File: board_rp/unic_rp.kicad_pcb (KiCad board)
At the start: 4 copper layers, 50 x 15.2 mm, 207 parts, among them J2 USB_C_Receptacle, Q1 2N7002, Q10 2N7002, Q11 2N7002, Q12 2N7002, Q13 2N7002, Q14 2N7002, Q15 2N7002, Q16 2N7002, Q17 2N7002, Q18 2N7002, Q19 2N7002, Q2 2N7002, Q20 2N7002, Q21 2N7002, Q22 2N7002, Q23 2N7002, Q24 2N7002, Q25 2N7002, Q26 2N7002, Q27 2N7002, Q28 2N7002, Q29 2N7002, Q3 2N7002, Q30 2N7002, Q31 2N7002, Q32 2N7002, Q33 2N7002, Q34 2N7002, Q35 2N7002, Q36 2N7002, Q37 2N7002, Q38 2N7002, Q39 2N7002, Q4 2N7002, Q40 2N7002, Q41 2N7002, Q42 AO3401A, Q43 2N7002, Q5 2N7002, Q6 2N7002, Q7 2N7002, Q8 2N7002, Q9 2N7002, U1 RP2350_80QFN, U10 ESD224DQA, U2 ESD224DQA, U3 MIC5203-3.3BM5, U4 APS6404L-3SQR-ZR, U5 TMUX154ERSW, U6 AP62150Z6, U7 W25Q16JVUXIQ, U8 LM393, U9 74AUP1G08, X1 27MHz

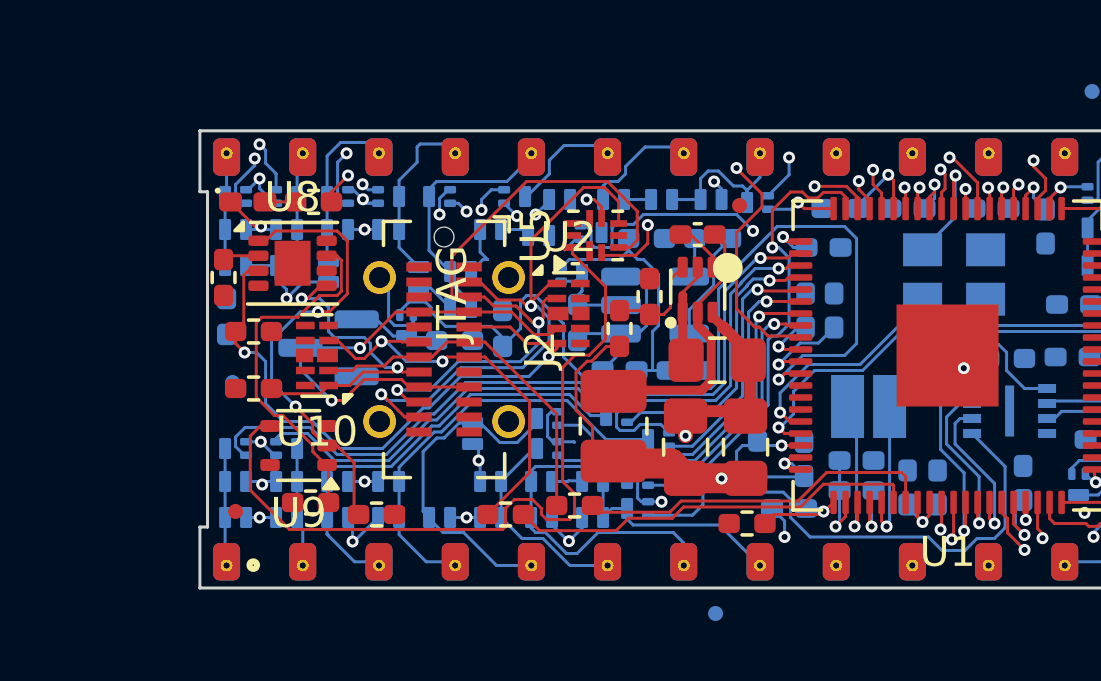
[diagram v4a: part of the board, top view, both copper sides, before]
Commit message: More or less complete schematic.
Component selection is not final, but functionality around
USB-C connector is. We even have UART output on it now as
well as USB VBUS detection and control on the right pins.
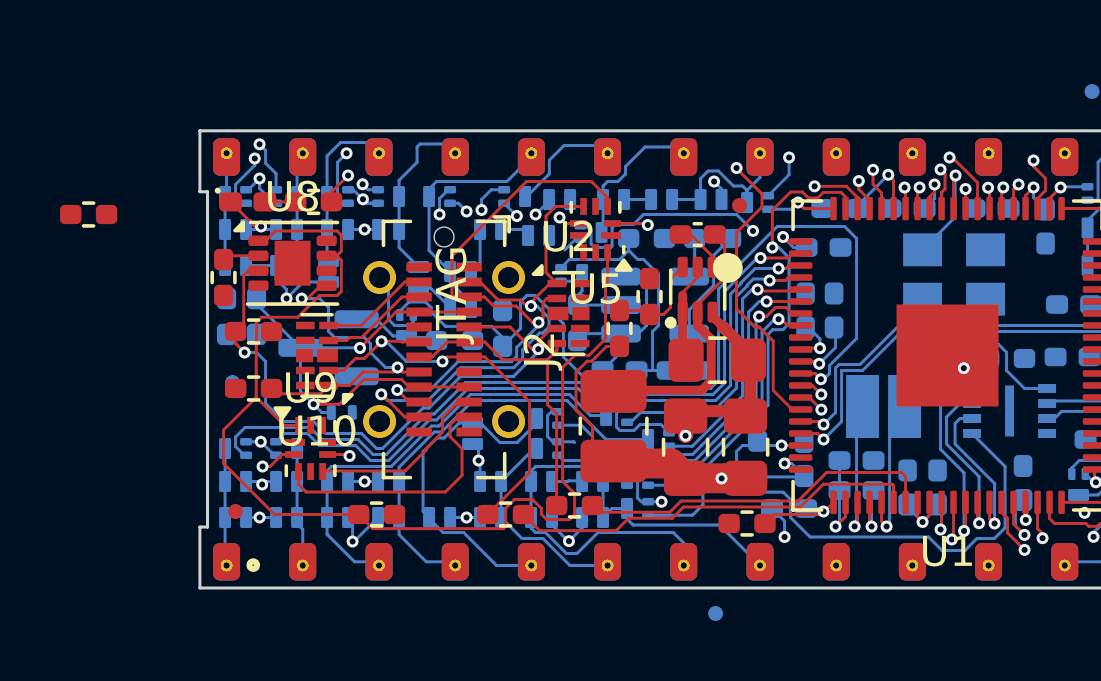
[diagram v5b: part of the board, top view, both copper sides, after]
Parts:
- added R27: 10k, UNIC:R_0402_1005Metric_Pad0.72x0.64mm_HandSolder, F.Cu at (34.6, 57.9)
- added U11: TPD1E05U06DPY, Package_SON:Texas_DPY0002A_0.6x1mm_P0.65mm, B.Cu at (43.0, 64.5)
- R23: value 10k -> 1k; moved to B.Cu
- U9: value 74AUP1G08 -> TMUX154ERSW; footprint Package_TO_SOT_SMD:SOT-353_SC-70-5 -> Package_DFN_QFN:UQFN-10_1.4x1.8mm_P0.4mm
- moved R23 6.46 mm to (40.2, 61.3), turned to 90 degrees
- moved L2 0.50 mm to (61.1, 64.3)
- moved U9 0.41 mm to (42.0, 65.7), turned to 0 degrees
- moved U5 0.20 mm to (51.5, 58.4), turned to 180 degrees
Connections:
- J2 pad A10: unconnected-(J2-RX2--PadA10) -> /USB_RXM
- J2 pad A11: unconnected-(J2-RX2+-PadA11) -> /USB_RXP
- J2 pad A2: /USB_TXM -> /USB_TXP
- J2 pad A3: /USB_TXP -> /USB_TXM
- J2 pad B10: unconnected-(J2-RX1--PadB10) -> /USB_RXM
- J2 pad B11: unconnected-(J2-RX1+-PadB11) -> /USB_RXP
- J2 pad B2: /USB_TXM -> /USB_TXP
- J2 pad B3: /USB_TXP -> /USB_TXM
- R1 pad 1: Net-(U1-GPIO40_ADC0) -> /LED_OUT
- R23 pad 1: +3V3 -> Net-(U1-GPIO40_ADC0)
- R23 pad 2: Net-(R23-Pad2) -> /VBUS
- R24 pad 2: Net-(R24-Pad2) -> Net-(U5-SEL)
- U1 pad 53: unconnected-(U1-GPIO42_ADC2-Pad53) -> /UART_TX
- U1 pad 54: unconnected-(U1-GPIO43_ADC3-Pad54) -> /UART_RX
- U1 pad 55: unconnected-(U1-GPIO44_ADC4-Pad55) -> /LED_OUT
- U10 pad 2: /USB_DP -> /USB_DM
- U10 pad 4: /USB_DM -> /USB_RXM
- U10 pad 5: unconnected-(U10-Pad5) -> /USB_RXP
- U2 pad 1: /USB_TXM -> /USB_TXP
- U2 pad 2: /USB_TXP -> /USB_TXM
- U2 pad 4: /VBUS -> /USB_CC1
- U2 pad 5: /USB_CC1 -> /USB_DP
- U5 pad 3: /USB_TXP -> /USB_TXM
- U5 pad 5: /USB_TXM -> /USB_TXP
- U8 pad 1: Net-(R24-Pad2) -> Net-(U5-SEL)
- U8 pad 7: Net-(R23-Pad2) -> Net-(U5-SEL)
- U9 pad 1: Net-(R23-Pad2) -> unconnected-(U9-A0-Pad1)
- U9 pad 2: Net-(R24-Pad2) -> /UART_RX
- U9 pad 3: GND -> /USB_RXP
- U9 pad 4: Net-(U5-SEL) -> GND
- U9 pad 5: +3V3 -> /USB_RXM
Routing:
- net /UART_RX: track 0.00 -> 27.6 mm, vias 0 -> 2
- net /LED_OUT: track 0.00 -> 24.4 mm, vias 0 -> 2
- net /UART_TX: track 0.00 -> 23.5 mm, vias 0 -> 2
- net Net-(U1-GPIO40_ADC0): track 22.4 -> 0.07 mm, vias 2 -> 0
- net Net-(R24-Pad2): track 15.4 -> 0.00 mm, vias 2 -> 0
- net Net-(U5-SEL): track 25.6 -> 39.3 mm
- net /USB_RXP: track 0.00 -> 12.4 mm
- net Net-(R23-Pad2): track 12.0 -> 0.00 mm
- net /USB_RXM: track 0.00 -> 9.78 mm
- net /USB_TXP: track 22.1 -> 16.9 mm
- net /USB_DP: track 12.0 -> 10.4 mm
- net /USB_PWR_EN: track 31.5 -> 30.1 mm
- net /SWCLK: track 13.2 -> 12.0 mm
- net +1V1: track 24.2 -> 23.2 mm
- net /SWD: track 12.6 -> 13.5 mm
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
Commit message: Component selection I think now is complete.
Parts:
- removed U11: TPD1E05U06DPY, Package_SON:Texas_DPY0002A_0.6x1mm_P0.65mm
- removed U5, U9: TMUX154ERSW, Package_DFN_QFN:UQFN-10_1.4x1.8mm_P0.4mm
- removed X1: 27MHz, UNIC:Oscillator_SMD_Abracon_ASE-4Pin_3.2x2.5mm
- added C2: 15p, UNIC:C_0402_1005Metric_Pad0.74x0.62mm_HandSolder, B.Cu at (60.4, 60.6)
- added C25: 15p, UNIC:C_0402_1005Metric_Pad0.74x0.62mm_HandSolder, B.Cu at (61.4, 59.3)
- added D21: PESD5V0L1BSLAZ, UNIC:D_SOD-882, F.Cu at (50.3, 58.9)
- added U12: 4066, Package_DFN_QFN:DHVQFN-14-1EP_2.5x3mm_P0.5mm_EP1x1.5mm, F.Cu at (41.2, 66.3)
- added Y1: 12MHz, UNIC:Oscillator_SMD_Abracon_ASE-4Pin_3.2x2.5mm, B.Cu at (63.9, 59.9)
- R23: moved to F.Cu
- U6: value AP62150Z6 -> TPS562242DRLR
- U8: footprint Package_SON:WSON-8-1EP_3x2.5mm_P0.5mm_EP1.2x1.5mm_PullBack -> Package_SON:WSON-8-1EP_2x2mm_P0.5mm_EP0.9x1.6mm
- moved R27 17.5 mm to (52.1, 58.8), turned to 180 degrees
- moved FID1 13.3 mm to (75.6, 64.8)
- moved R23 12.4 mm to (52.1, 57.8), turned to 180 degrees
- moved FID4 6.61 mm to (46.1, 68.2)
- moved R26 3.71 mm to (42.7, 59.1), turned to 90 degrees
- moved FID7 3.61 mm to (55.8, 67.6)
- moved R25 1.00 mm to (40.2, 61.4)
- moved U8 0.86 mm to (40.6, 59.2)
- moved R6 0.80 mm to (40.1, 62.9)
- moved FID5 0.30 mm to (39.4, 63.2)
- moved FID8 0.22 mm to (56.5, 57.5)
- moved D79 0.20 mm to (42.8, 59.8)
- moved D80 0.10 mm to (43.0, 58.4)
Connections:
- U1 pad 31: unconnected-(U1-XOUT-Pad31) -> Net-(U1-XOUT)
- U8 pad 9: (no net) -> GND
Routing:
- net /SWCLK: track 12.0 -> 32.7 mm
- net /SWD: track 13.5 -> 33.1 mm
- net Net-(U1-GPIO40_ADC0): track 0.07 -> 12.7 mm
- net Net-(R24-Pad2): track 39.3 -> 29.0 mm, vias 0 -> 2
- net Net-(U8A--): track 1.22 -> 10.3 mm, vias 0 -> 2
- net /CLK1: track 4.06 -> 10.3 mm
- net Net-(U1-XOUT): track 0.00 -> 5.89 mm, vias 0 -> 1
- net /USB_TXP: track 16.9 -> 22.2 mm, vias 2 -> 4
- net /UART_RX: track 27.6 -> 22.8 mm
- net +5V: track 66.5 -> 70.2 mm
- net /VBUS: track 16.8 -> 20.4 mm
- net /USB_TXM: track 19.3 -> 15.8 mm
- net GND: track 57.8 -> 61.3 mm
- net LINE: track 35.4 -> 37.9 mm
- net /USB_CC1: track 20.4 -> 22.2 mm
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
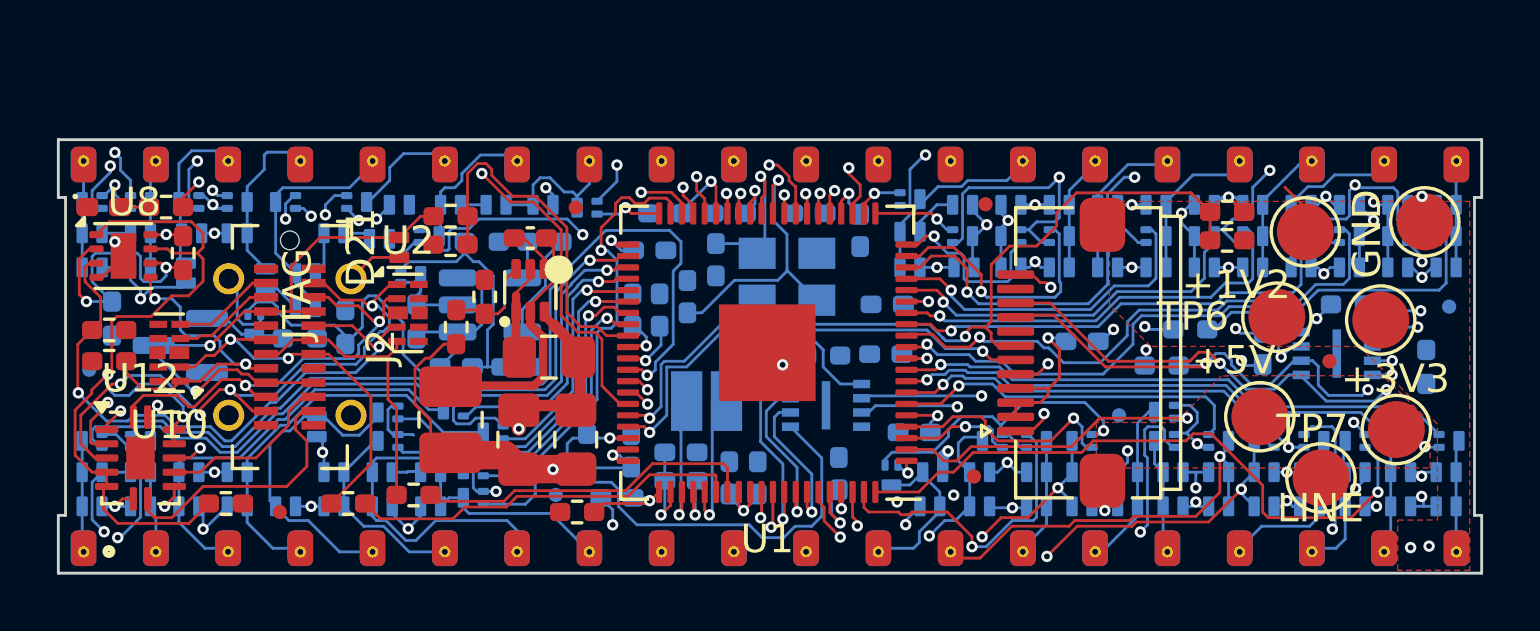
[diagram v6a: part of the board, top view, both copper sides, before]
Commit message: Board fully routed except for power.
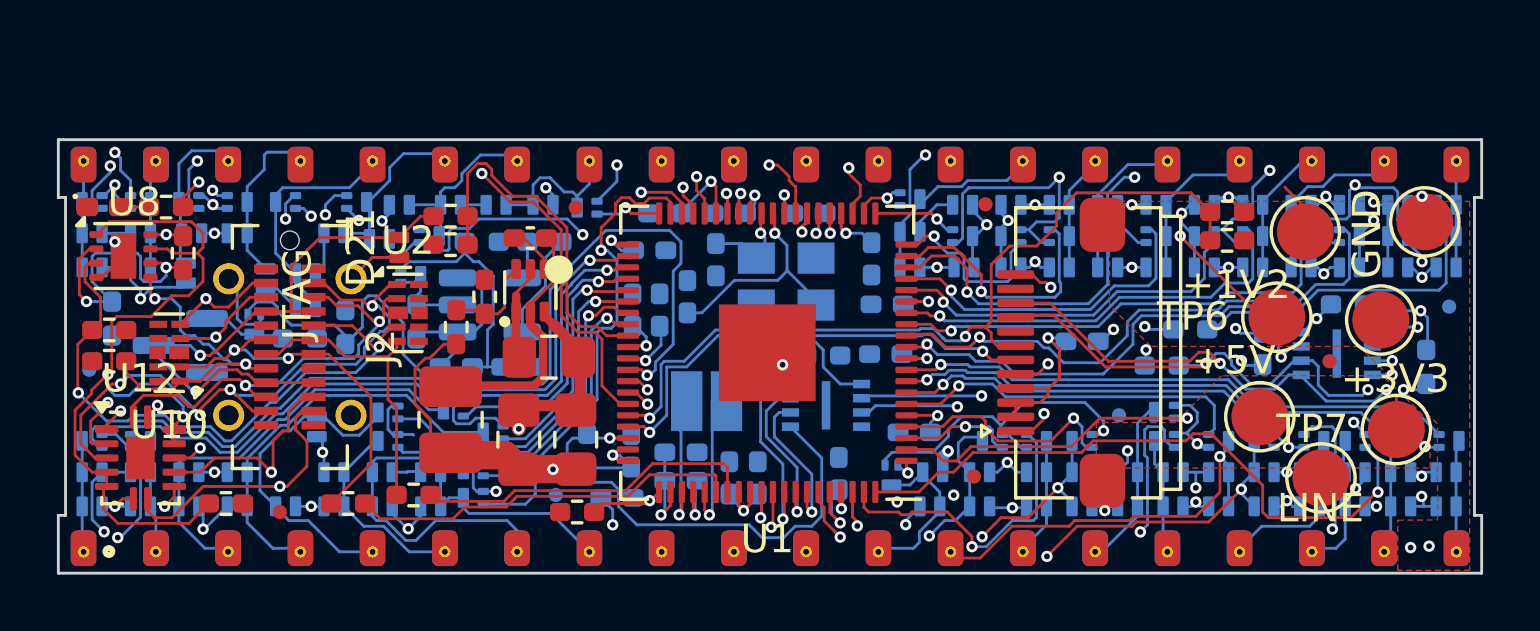
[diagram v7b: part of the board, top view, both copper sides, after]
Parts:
- moved C16 1.08 mm to (66.9, 59.3)
- moved Y1 0.17 mm to (63.9, 60.1)
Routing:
- net Net-(U1-RUN): track 2.74 -> 25.8 mm, vias 1 -> 2
- net /USB_RXP: track 13.5 -> 21.9 mm, vias 0 -> 2
- net +1V1: track 23.2 -> 15.4 mm
- net /USB_RXM: track 9.90 -> 17.1 mm, vias 0 -> 2
- net Net-(U1-XOUT): track 5.89 -> 3.41 mm
- net Net-(R21-Pad1): track 0.00 -> 2.39 mm, vias 0 -> 1
- net /CLK1: track 10.3 -> 7.98 mm
- net /FLASH_CS_N: track 35.1 -> 36.6 mm
- net /PIN35: track 4.86 -> 6.21 mm
- net /PIN34: track 5.03 -> 6.13 mm
- net /PIN35_F: track 21.7 -> 20.7 mm
